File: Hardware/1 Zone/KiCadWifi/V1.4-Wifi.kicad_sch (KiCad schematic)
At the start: 129 parts, among them CN11 Pinheader 1x02 P2.54 Horizont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, CN16 Pinheader 1x02 P2.54 Horizont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, Q1 AOD4184A, Q10 PJA3404A, Q11 PJA3404A, Q12 BC816-16VL, Q8 UMH3NTN, SW1 K2-1102DP-G3SW-04, SW2 K2-1102DP-G3SW-04, SW3 K2-1102DP-G3SW-04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

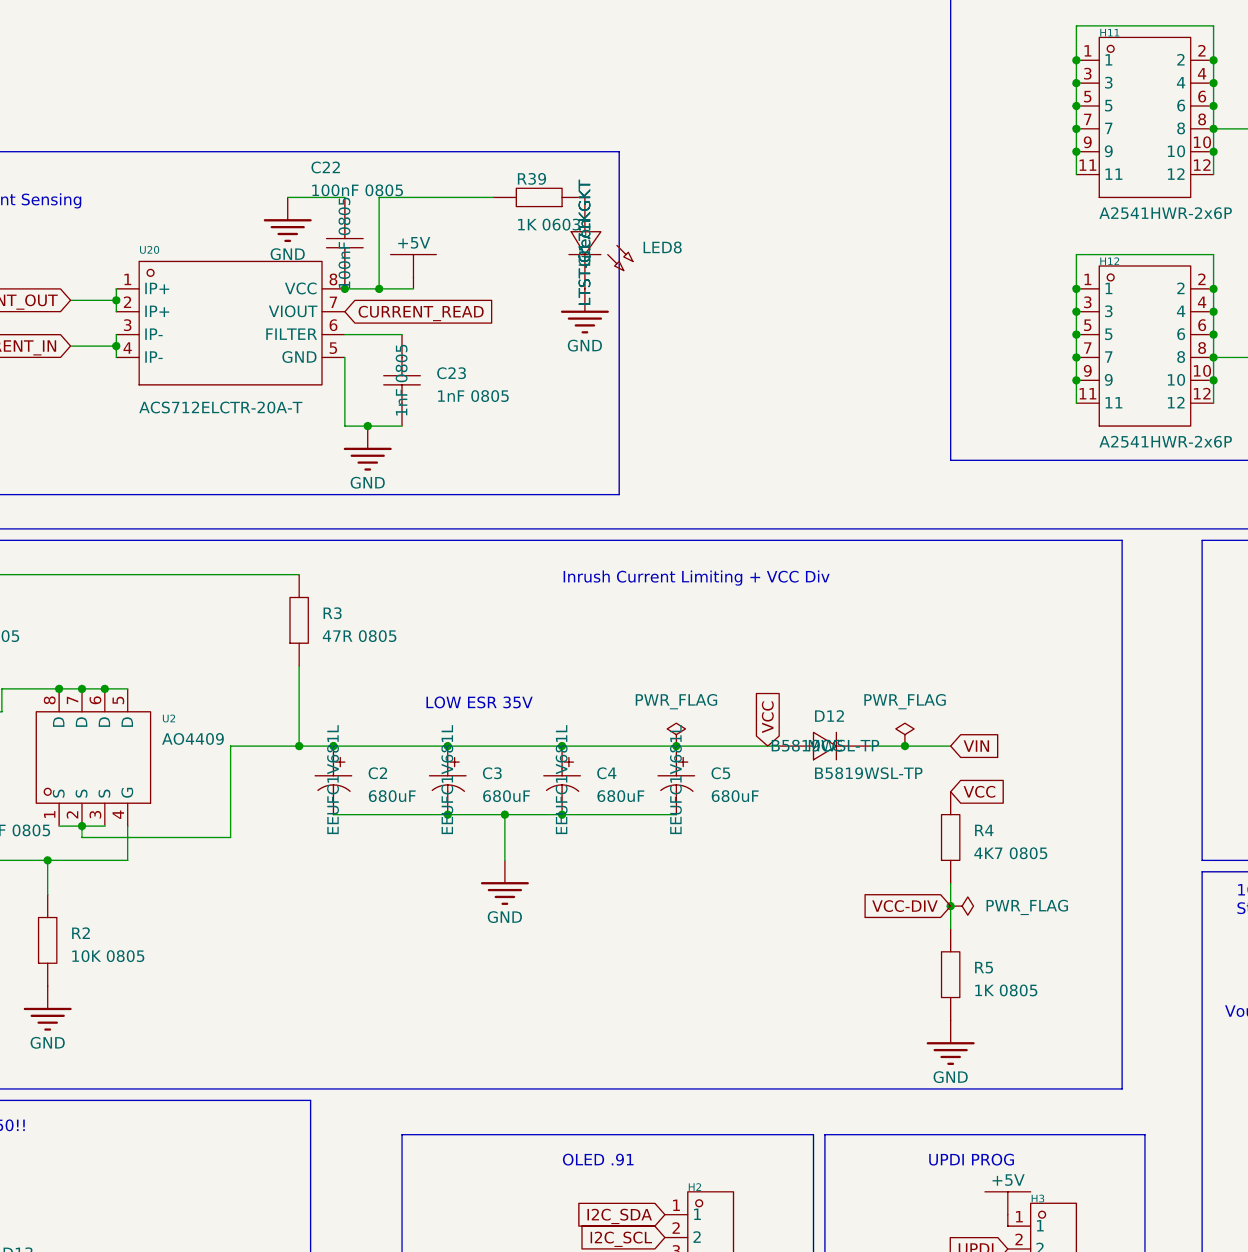
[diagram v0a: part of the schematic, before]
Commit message: Replaced part U2 from AO4409 to DMPH4015SSSQ
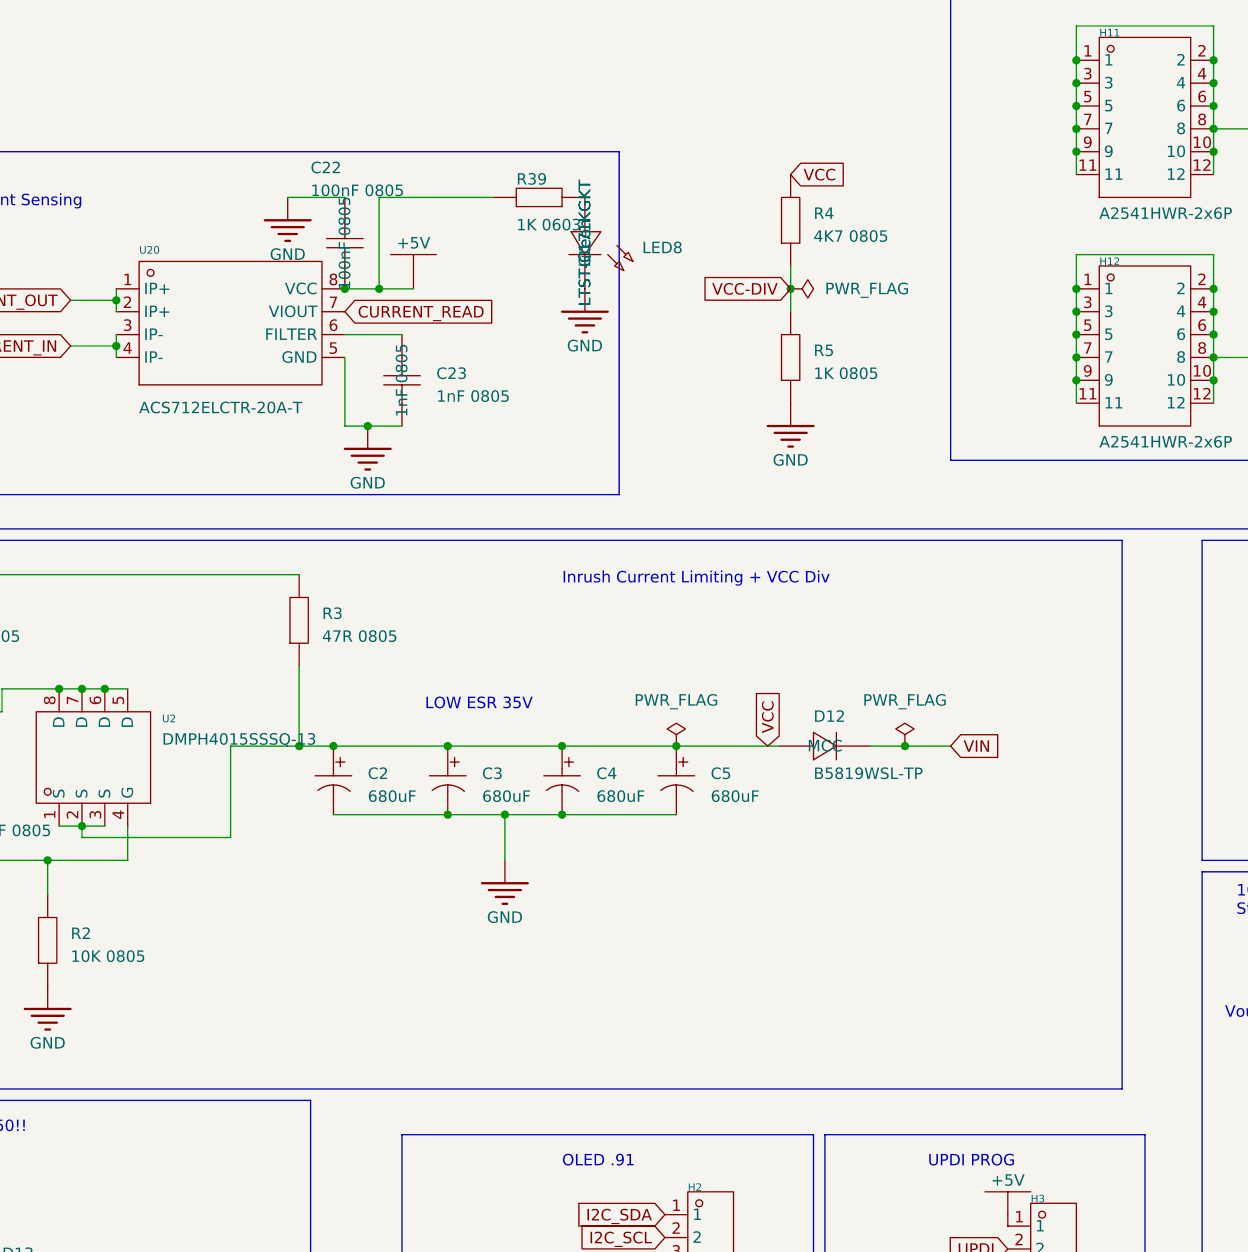
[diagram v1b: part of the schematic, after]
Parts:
- U2: value AO4409 -> DMPH4015SSSQ-13; footprint V1.4-Wifi-easyedapro:SOP-8_L4.9-W3.9-P1.27-LS6.0-BL -> Package_SO:SOIC-8_3.9x4.9mm_P1.27mm; LCSC Part Name AO4409 -> (none); MPN (none) -> DMPH4015SSSQ-13; Manufacturer TECHPUBLIC(台舟) -> (none); Manufacturer Part AO4409 -> (none); Supplier LCSC -> (none); Supplier Part C7603375 -> (none)
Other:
- moved on the sheet: R4, R5

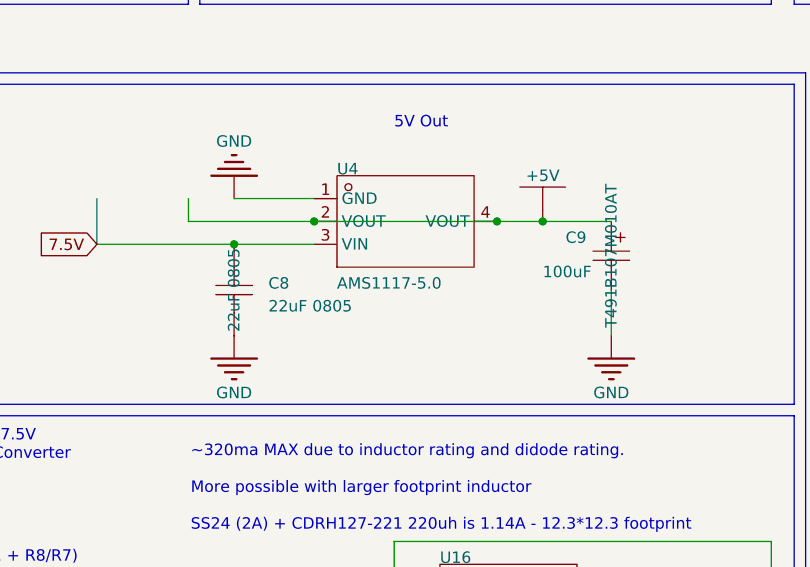
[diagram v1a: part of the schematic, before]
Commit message: Replaced U4 from AMS1117-5.0 to LDI1117-05H
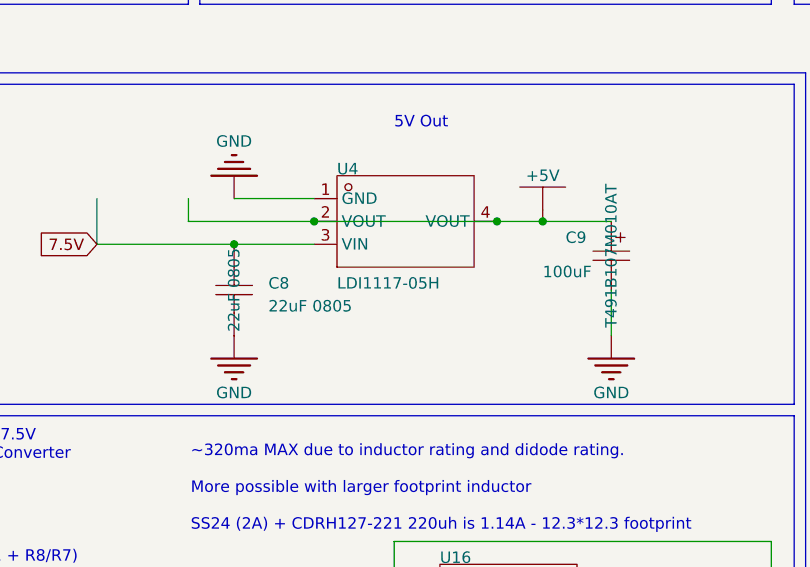
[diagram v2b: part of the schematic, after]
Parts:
- U4: value AMS1117-5.0 -> LDI1117-05H; footprint V1.4-Wifi-easyedapro:SOT-223-3_L6.7-W3.7-P2.30-LS7.0-BR -> Package_TO_SOT_SMD:SOT-223; LCSC Part Name AMS1117-5.0SOT-223 -> (none); MPN (none) -> LDI1117-05H; Manufacturer JSMSEMI(杰盛微) -> (none); Manufacturer Part AMS1117-5.0 -> (none); Supplier LCSC -> (none); Supplier Part C917153 -> (none)

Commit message: Replaced U15 from AMS1117-3.3 to LD1117S33CTR
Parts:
- U11, U22: MPN (none) -> CH340C
- U15: value AMS1117-3.3 -> LD1117S33CTR; footprint V1.4-Wifi-easyedapro:SOT-223-3_L6.5-W3.4-P2.30-LS7.0-BR -> Package_TO_SOT_SMD:SOT-223; Company (none) -> STMicroelectronics; LCSC Part Name 输出3.3V1A -> (none); MPN (none) -> LD1117S33CTR; Manufacturer AMS -> (none); Manufacturer Part AMS1117-3.3 -> (none); Supplier LCSC -> (none); Supplier Part C6186 -> (none)
- U9: LCSC Part Name WT8266-S5ESP-12F -> (none); Manufacturer Wireless-tag(启明云端) -> (none); Supplier LCSC -> (none); Supplier Part C477829 -> (none)

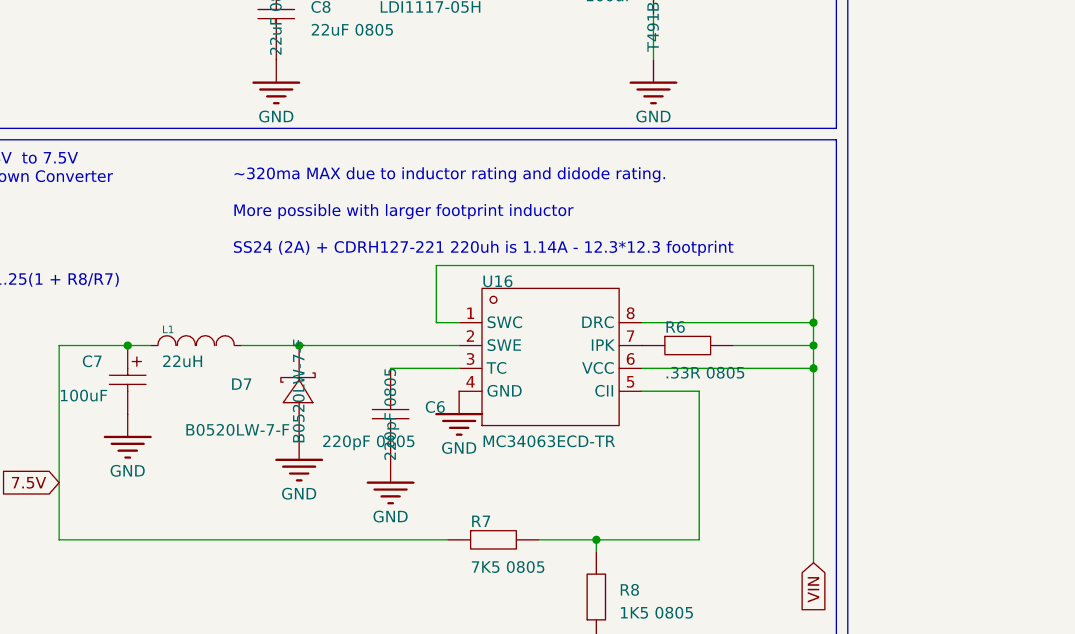
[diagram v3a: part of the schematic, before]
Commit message: Upgraded L1 (MSS1048-104MLC) and D7 (SK34SMA-3G). Layout changes to accomodate larger footprints.
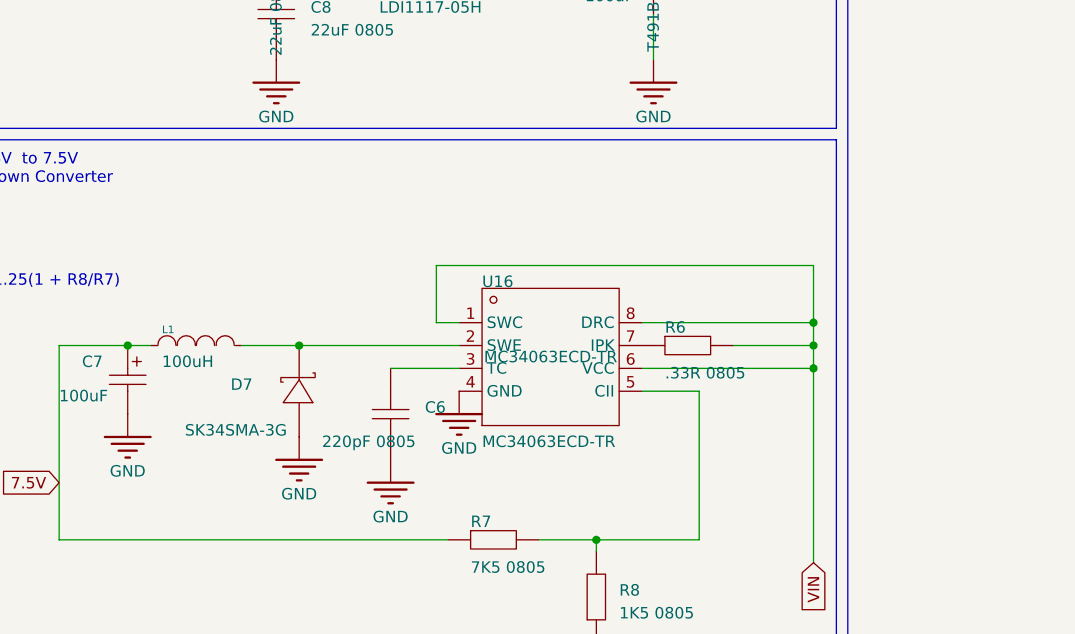
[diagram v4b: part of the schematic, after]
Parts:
- D7: value B0520LW-7-F -> SK34SMA-3G; footprint V1.4-Wifi-easyedapro:SOD-123_L2.8-W1.8-LS3.7-RD -> Diode_SMD:D_SMA_Handsoldering; LCSC Part Name 20V500mA450mV@500mA -> (none); MPN B0520LW-7-F -> SK34SMA-3G; Manufacturer Diodes Incorporated -> Diotec Semiconductor; Manufacturer Part B0520LW-7-F -> SK34SMA-3G; Supplier LCSC -> (none); Supplier Part C77335 -> (none)
- L1: value 22uH -> 100uH; footprint Inductor_SMD:L_TDK_SLF6045 -> Inductor_SMD:L_Coilcraft_MSS1048-XXX; MPN (none) -> MSS1048-104MLC; Manufacturer TDK -> Coilcraft; Manufacturer Part VLS6045EX-220M-H -> MSS1048-104MLC
- U16: footprint V1.4-Wifi-easyedapro:SOIC-8_L5.0-W4.0-P1.27-LS6.0-BL -> Package_SO:SOIC-8_3.9x4.9mm_P1.27mm; MPN (none) -> MC34063ECD-TR; Manufacturer ST(意法半导体) -> STMicro
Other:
- note removed: "~320ma MAX due to inductor rating and didode rating. More possible with larger footprint inductor SS24 (2A) + CDRH127-221 220uh is 1.14A - 12.3*12.3 footprint"

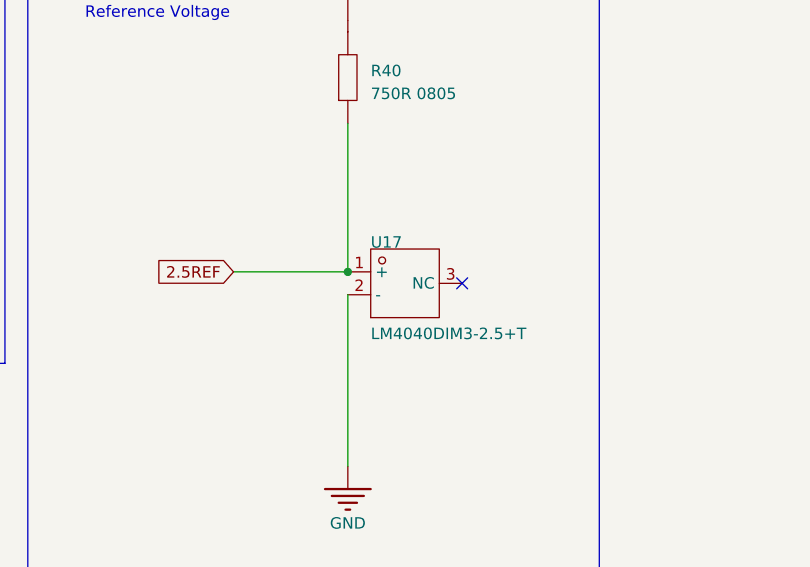
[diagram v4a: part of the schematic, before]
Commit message: Replaced U17 custom footprint with standard
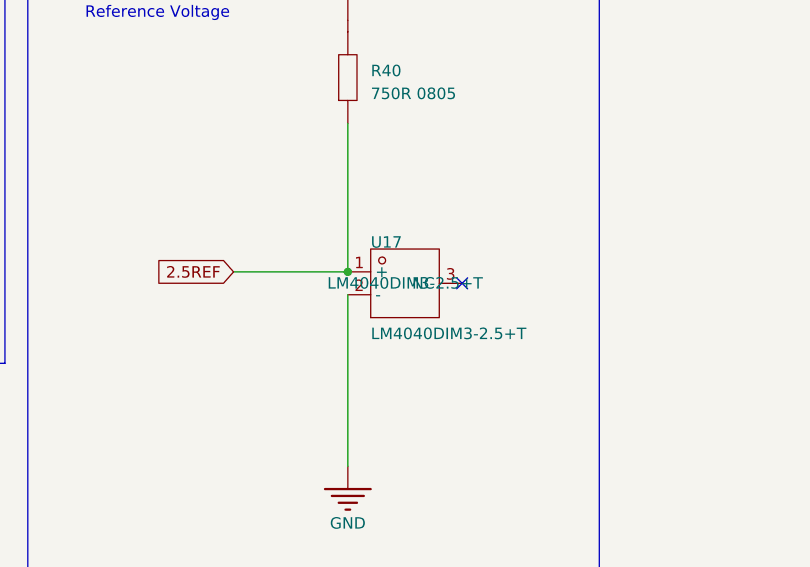
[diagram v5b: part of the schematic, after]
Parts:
- U17: footprint V1.4-Wifi-easyedapro:SOT-23-3_L2.9-W1.6-P1.90-LS2.8-BR -> Package_TO_SOT_SMD:SOT-23-3; MPN (none) -> LM4040DIM3-2.5+T; Manufacturer ADI(亚德诺) -> Analog Devices

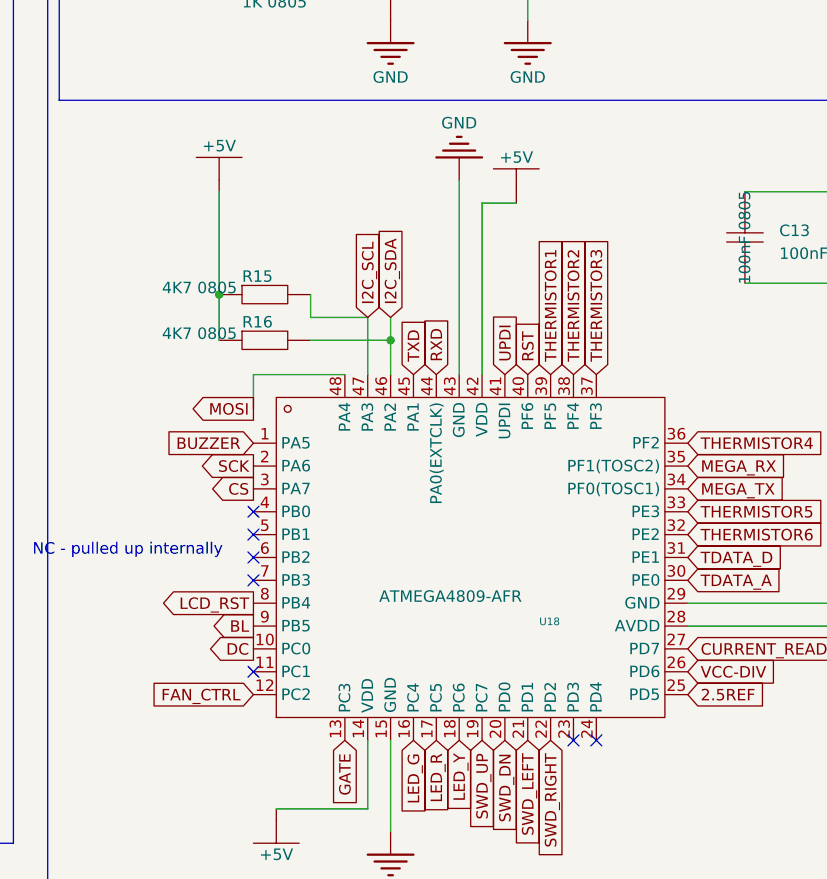
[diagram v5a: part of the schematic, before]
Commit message: Replaced U18 AtMega footprint with center pad. A bit of rerouting and GND stitching for EMC improvements (shrink GND loops)
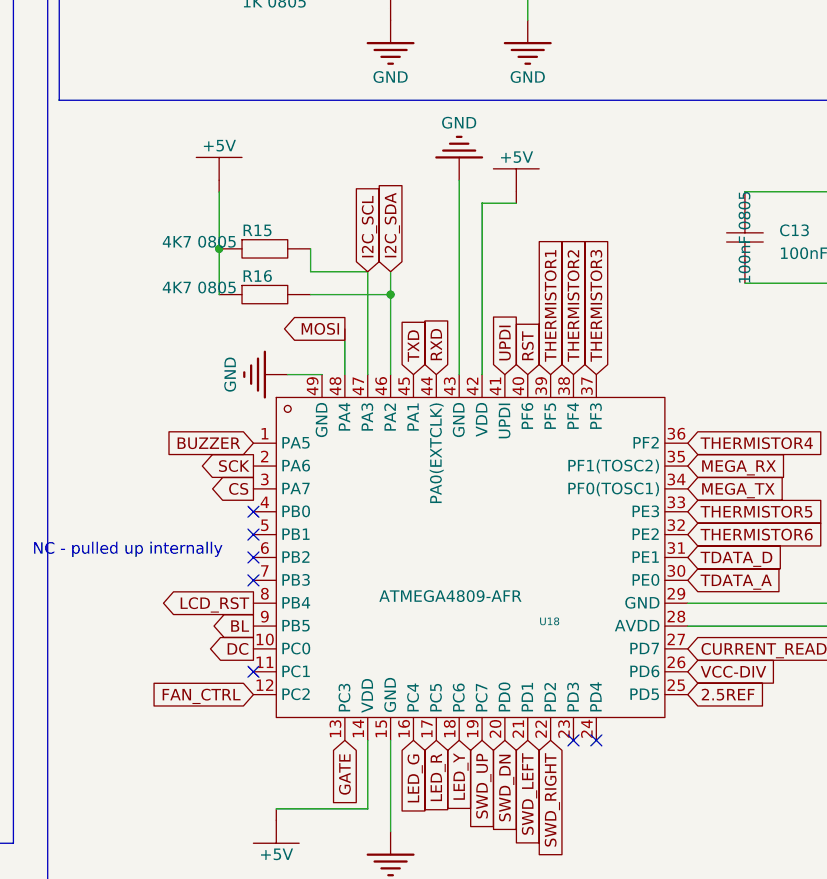
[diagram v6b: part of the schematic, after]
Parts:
- U18: footprint V1.4-Wifi-easyedapro:TQFP-48_L7.0-W7.0-P0.50-LS9.0-BL -> Package_QFP:TQFP-48-1EP_7x7mm_P0.5mm_EP3.5x3.5mm; JLCPCB Part Class ExtendedPart -> (none); LCSC Part Name ATMEGA4809-AFR -> (none); Manufacturer MICROCHIP(美国微芯) -> MICROCHIP; Supplier LCSC -> (none); Supplier Part C189475 -> (none)
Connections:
- net GND: now also U18.49 (GND)
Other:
- moved on the sheet: R15, R16

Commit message: Replaced USB1, USB2 to 10118193-0001LF
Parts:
- U18: MPN (none) -> ATMEGA4809-AFR
- U20: MPN (none) -> ACS712ELCTR-20A-T
- USB1: value U254-051T-4BH83-S1S -> 10118193-0001LF; footprint V1.4-Wifi-easyedapro:MICRO-USB-SMD_U254-051T-4BH83-S1S -> Connector_USB:USB_Micro-B_Amphenol_10118193-0001LF_Horizontal; LCSC Part Name Micro-B母座卧贴 -> (none); MPN (none) -> 10118193-0001LF; Manufacturer XKBConnectivity(中国星坤) -> Amphenol; Manufacturer Part U254-051T-4BH83-S1S -> 10118193-0001LF; Supplier LCSC -> (none); Supplier Part C319160 -> (none)
- USB2: value U254-051T-4BH83-S1S -> 10118193-0001LF; footprint V1.4-Wifi-easyedapro:MICRO-USB-SMD_U254-051T-4BH83-S1S -> Connector_USB:USB_Micro-B_Amphenol_10118193-0001LF_Horizontal; MPN (none) -> 10118193-0001LF; Manufacturer XKBConnectivity(中国星坤) -> Amphenol; Manufacturer Part U254-051T-4BH83-S1S -> 10118193-0001LF

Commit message: Replace Buzzer1 with CMT-8504-100-SMT-TR
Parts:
- BUZZER1: footprint V1.4-Wifi-easyedapro:BUZ-SMD_4P-L8.5-W8.5-P8.50-BR -> Buzzer_Beeper:MagneticBuzzer_CUI_CMT-8504-100-SMT; LCSC Part Name MLT-8530 -> (none); Manufacturer 华能 -> Same Sky; Manufacturer Part MLT-8530 -> CMT-8530S-SMT-TRCMT-8504-100-SMT-TR; Supplier LCSC -> (none); Supplier Part C94599 -> (none)
